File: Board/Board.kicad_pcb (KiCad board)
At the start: 4 copper layers, 24 x 46 mm, 49 parts, among them J1 Conn_01x03, U1 USB-C, U13 ESP32-C6-MINI-1-N4, U3 AHT20, U4 Tactile-Switch, U6 Light sensor, U7 Tactile-Switch, U8 Slide-Switch, U9 Battery-Spring

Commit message: Add missing tabs to blumy panel
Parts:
- added U14: ~, CustomFootprints:MouseBites5mm, F.Cu at (164.0, 227.3)
- added U5: ~, CustomFootprints:MouseBites5mm, F.Cu at (177.0, 227.3)

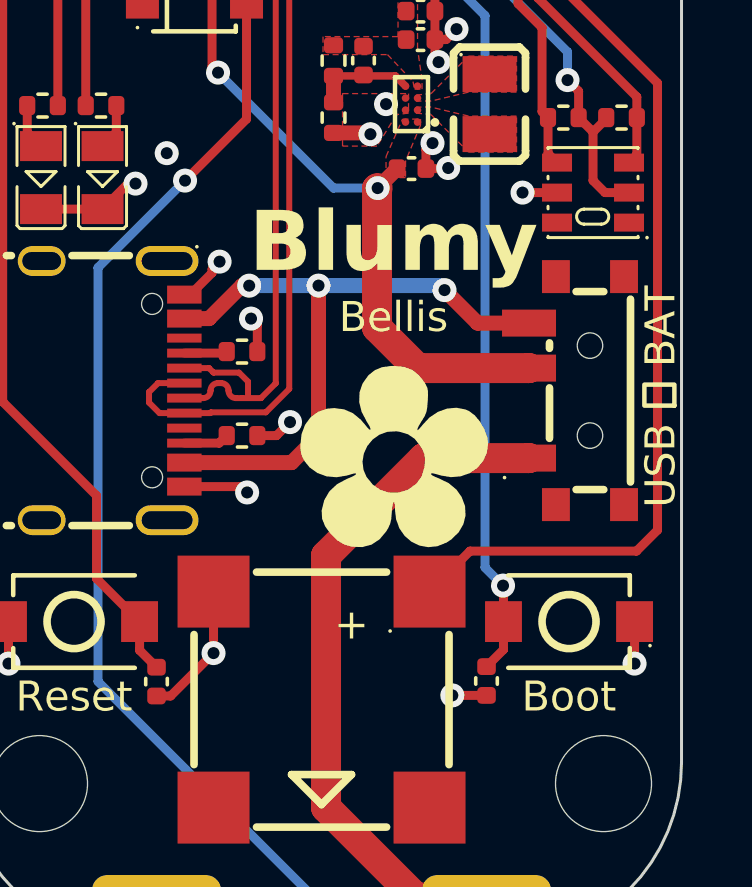
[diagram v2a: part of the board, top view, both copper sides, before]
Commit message: Remove boot capacitor from blumy and flip usb bat text
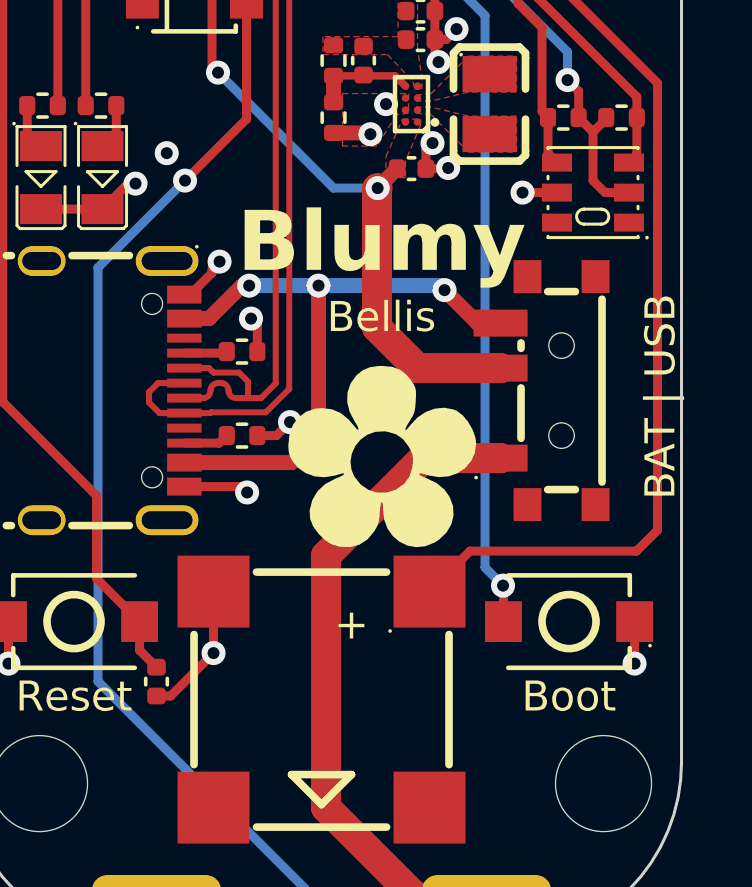
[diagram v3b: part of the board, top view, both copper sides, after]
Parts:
- removed C5: 100nF-Ceramic, Capacitor_SMD:C_0402_1005Metric
- moved U8 0.95 mm to (177.6, 155.4)
- moved Flower1 0.40 mm to (172.0, 157.5)
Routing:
- net IO9: track 27.7 -> 25.9 mm
- net GND: track 225.3 -> 224.1 mm, vias 42 -> 41
- net PWR_VIN: track 22.2 -> 21.3 mm
- net PWR_USB_VIN: track 22.3 -> 21.4 mm
- net PWR_BAT_VIN: track 23.1 -> 22.2 mm
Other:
- board text added: "BAT | USB"
- board text removed: "USB 〡 BAT"
